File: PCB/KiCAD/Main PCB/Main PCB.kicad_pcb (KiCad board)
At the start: 2 copper layers, 118 x 118 mm, 127 parts, among them IC1 ADG608BRZ, IC2 ADG608BRZ, IC3 VNH7070ASTR, IC4 VNH7070ASTR, IC5 VNH7070ASTR, IC6 VNH7070ASTR, IC7 VNH7070ASTR, IC8 XB3-24Z8CM, J1 Conn_01x04, J2 Conn_01x04, J3 Conn_01x04, J4 Conn_01x04, J5 Conn_01x02, J6 Conn_01x02, J7 Conn_Coaxial_Small, J8 Conn_01x02, J9 Conn_01x02, M1 Conn_01x02, M2 Conn_01x02, M3 Conn_01x02, M4 Conn_01x02, Q1 BSS138, Q2 BSS138, U1 Teensy4.1, U2 Teensy4.0

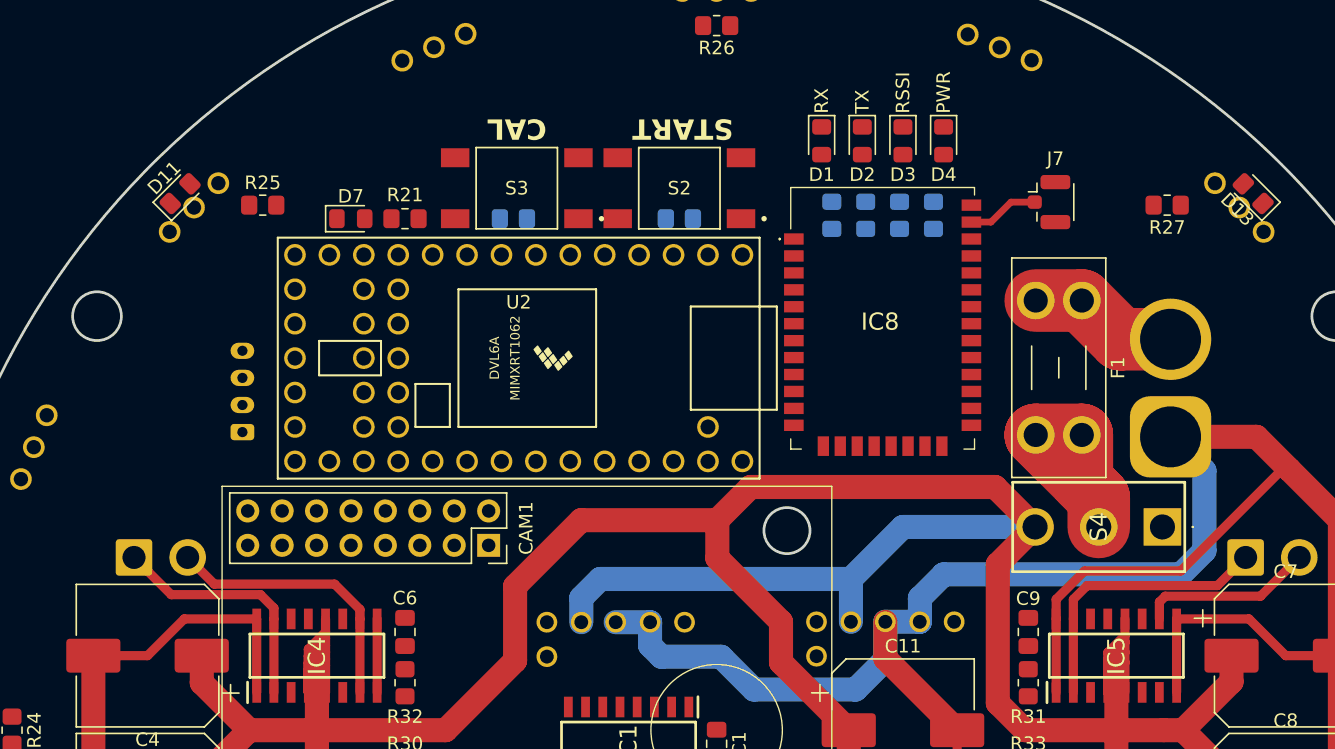
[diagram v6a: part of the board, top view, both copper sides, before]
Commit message: Changed to PCB and CAD
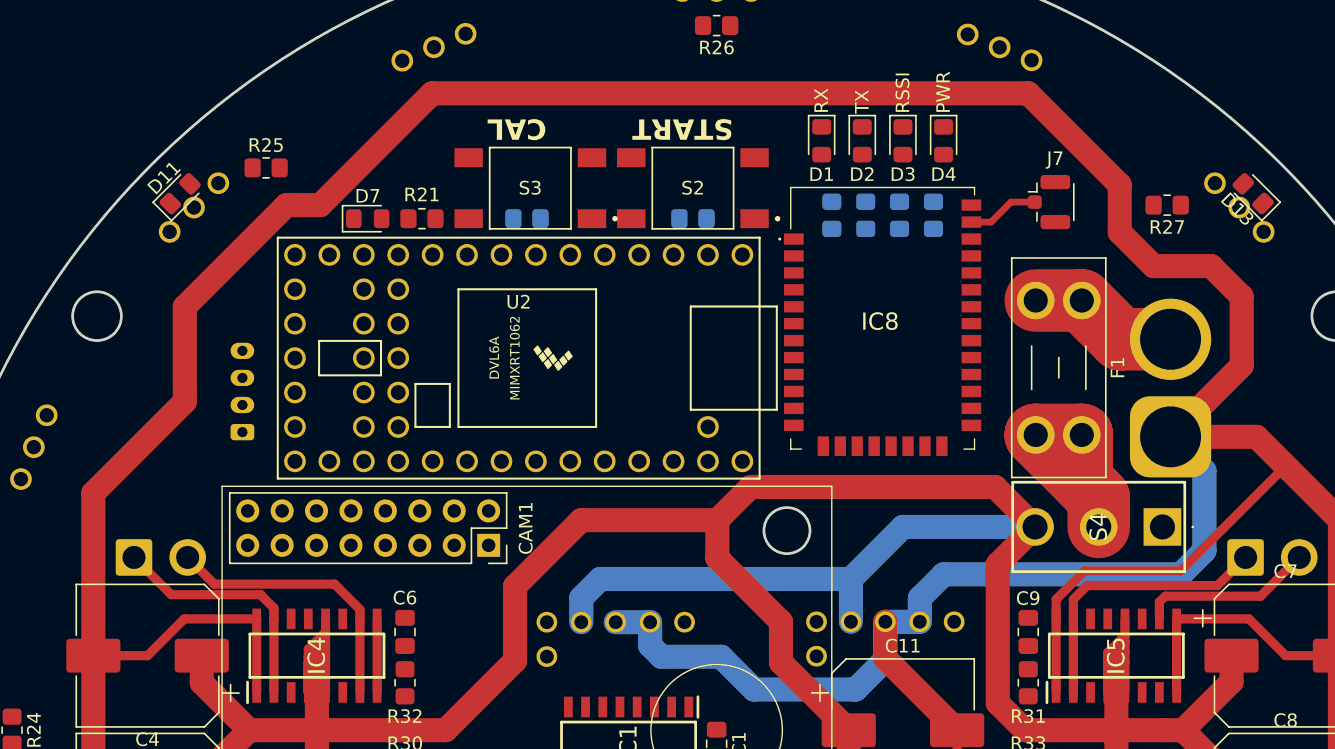
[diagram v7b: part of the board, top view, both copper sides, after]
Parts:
- moved R25 2.76 mm to (-33.2, -41.5)
- moved D7 1.25 mm to (-25.8, -37.8)
- moved R21 1.25 mm to (-21.8, -37.8)
- moved R3 1.00 mm to (-1.75, -37.8)
- moved R4 1.00 mm to (-14.0, -37.8)
- moved S2 1.00 mm to (-1.75, -40.0)
- moved S3 1.00 mm to (-13.8, -40.0)
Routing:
- net GND: track 351.7 -> 485.5 mm
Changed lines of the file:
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@@
 			(psa4output no)
 			(plot_black_and_white yes)
+			(plotinvisibletext no)
 			(sketchpadsonfab no)
 			(plotpadnumbers no)
@@
 	(footprint "TS04:SW_TS04-66-70-BK-260-SMT"
 		(layer "F.Cu")
-		(at -14.75 -40 180)
+		(at -13.75 -40 180)
 		(property "Reference" "S3"
 			(at 0 0 0)
@@
 	(footprint "Resistor_SMD:R_0805_2012Metric_Pad1.20x1.40mm_HandSolder"
 		(layer "F.Cu")
-		(at -33.5 -38.75)
+		(at -33.25 -41.5)
 		(descr "Resistor SMD 0805 (2012 Metric), square (rectangular) end terminal, IPC_7351 nominal with elongated pad for handsoldering. (Body size source: IPC-SM-782 page 72, https://www.pcb-3d.com/wordpress/wp-content/uploads/ipc-sm-782a_amendment_1_and_2.pdf), generated with kicad-footprint-generator")
 		(tags "resistor handsolder")
@@
 	(footprint "LED_SMD:LED_0805_2012Metric_Pad1.15x1.40mm_HandSolder"
 		(layer "F.Cu")
-		(at -27 -37.75)
+		(at -25.75 -37.75)
 		(descr "LED SMD 0805 (2012 Metric), square (rectangular) end terminal, IPC_7351 nominal, (Body size source: https://docs.google.com/spreadsheets/d/1BsfQQcO9C6DZCsRaXUlFlo91Tg2WpOkGARC1WS5S8t0/edit?usp=sharing), generated with kicad-footprint-generator")
 		(tags "LED handsolder")
@@
 	(footprint "TS04:SW_TS04-66-70-BK-260-SMT"
 		(layer "F.Cu")
-		(at -2.75 -40 180)
+		(at -1.75 -40 180)
 		(property "Reference" "S2"
 			(at 0 0 0)
@@
 	(footprint "Resistor_SMD:R_0805_2012Metric_Pad1.20x1.40mm_HandSolder"
 		(layer "F.Cu")
-		(at -23 -37.75 180)
+		(at -21.75 -37.75 180)
 		(descr "Resistor SMD 0805 (2012 Metric), square (rectangular) end terminal, IPC_7351 nominal with elongated pad for handsoldering. (Body size source: IPC-SM-782 page 72, https://www.pcb-3d.com/wordpress/wp-content/uploads/ipc-sm-782a_amendment_1_and_2.pdf), generated with kicad-footprint-generator")
 		(tags "resistor handsolder")
@@
 	(footprint "Resistor_SMD:R_0805_2012Metric_Pad1.20x1.40mm_HandSolder"
 		(layer "B.Cu")
-		(at -2.75 -37.75)
+		(at -1.75 -37.75)
 		(descr "Resistor SMD 0805 (2012 Metric), square (rectangular) end terminal, IPC_7351 nominal with elongated pad for handsoldering. (Body size source: IPC-SM-782 page 72, https://www.pcb-3d.com/wordpress/wp-content/uploads/ipc-sm-782a_amendment_1_and_2.pdf), generated with kicad-footprint-generator")
 		(tags "resistor handsolder")
@@
 	(footprint "Resistor_SMD:R_0805_2012Metric_Pad1.20x1.40mm_HandSolder"
 		(layer "B.Cu")
-		(at -15 -37.75)
+		(at -14 -37.75)
 		(descr "Resistor SMD 0805 (2012 Metric), square (rectangular) end terminal, IPC_7351 nominal with elongated pad for handsoldering. (Body size source: IPC-SM-782 page 72, https://www.pcb-3d.com/wordpress/wp-content/uploads/ipc-sm-782a_amendment_1_and_2.pdf), generated with kicad-footprint-generator")
 		(tags "resistor handsolder")
@@
 	)
 	(segment
+		(start -39.25 -24.25)
+		(end -39.25 -31.25)
+		(width 1.78)
+		(layer "F.Cu")
+		(net 1)
+	)
+	(segment
 		(start 25.055 -8.212)
 		(end 25.055 -2.788)
@@
 	)
 	(segment
+		(start -31.75 -38.75)
+		(end -29.25 -38.75)
+		(width 1.78)
+		(layer "F.Cu")
+		(net 1)
+	)
+	(segment
+		(start 32.25 -34.25)
+		(end 36.5 -34.25)
+		(width 1.78)
+		(layer "F.Cu")
+		(net 1)
+	)
+	(segment
 		(start -45 15)
 		(end -46 14)
@@
 	)
 	(segment
+		(start 38.75 -32)
+		(end 38.75 -26.9)
+		(width 1.78)
+		(layer "F.Cu")
+		(net 1)
+	)
+	(segment
 		(start 44.5 15.75)
 		(end 40 15.75)
@@
 	)
 	(segment
+		(start 38.75 -26.9)
+		(end 33.5 -21.65)
+		(width 1.78)
+		(layer "F.Cu")
+		(net 1)
+	)
+	(segment
+		(start 29.75 -40.25)
+		(end 29.75 -36.75)
+		(width 1.78)
+		(layer "F.Cu")
+		(net 1)
+	)
+	(segment
 		(start 41.75 -19.25)
 		(end 42.25 -19.25)
@@
 	)
 	(segment
+		(start -46 -17.5)
+		(end -39.25 -24.25)
+		(width 1.78)
+		(layer "F.Cu")
+		(net 1)
+	)
+	(segment
 		(start 27.1505 -11.75)
 		(end 34.25 -11.75)
@@
 	)
 	(segment
+		(start -21 -47)
+		(end 23 -47)
+		(width 1.78)
+		(layer "F.Cu")
+		(net 1)
+	)
+	(segment
 		(start 33.945 2.788)
 		(end 33.945 8.212)
@@
 	)
 	(segment
+		(start 36.5 -34.25)
+		(end 38.75 -32)
+		(width 1.78)
+		(layer "F.Cu")
+		(net 1)
+	)
+	(segment
 		(start 17.75 0.5)
 		(end 17.25 0)
@@
 	)
 	(segment
+		(start -46 -5.5)
+		(end -46 -17.5)
+		(width 1.78)
+		(layer "F.Cu")
+		(net 1)
+	)
+	(segment
 		(start -33.945 2.788)
 		(end -33.945 8.212)
@@
 	)
 	(segment
+		(start 29.75 -36.75)
+		(end 32.25 -34.25)
+		(width 1.78)
+		(layer "F.Cu")
+		(net 1)
+	)
+	(segment
 		(start 46 5.5)
 		(end 46 14.25)
@@
 	)
 	(segment
+		(start -29.25 -38.75)
+		(end -21 -47)
+		(width 1.78)
+		(layer "F.Cu")
+		(net 1)
+	)
+	(segment
 		(start 34.25 -11.75)
 		(end 41.75 -19.25)
@@
 	)
 	(segment
+		(start -39.25 -31.25)
+		(end -31.75 -38.75)
+		(width 1.78)
+		(layer "F.Cu")
+		(net 1)
+	)
+	(segment
 		(start -26.6505 11.25)
 		(end -35.5 11.25)
@@
 		(layer "F.Cu")
 		(net 1)
+	)
+	(segment
+		(start 23 -47)
+		(end 29.75 -40.25)
+		(width 1.78)
+		(layer "F.Cu")
+		(net 1)

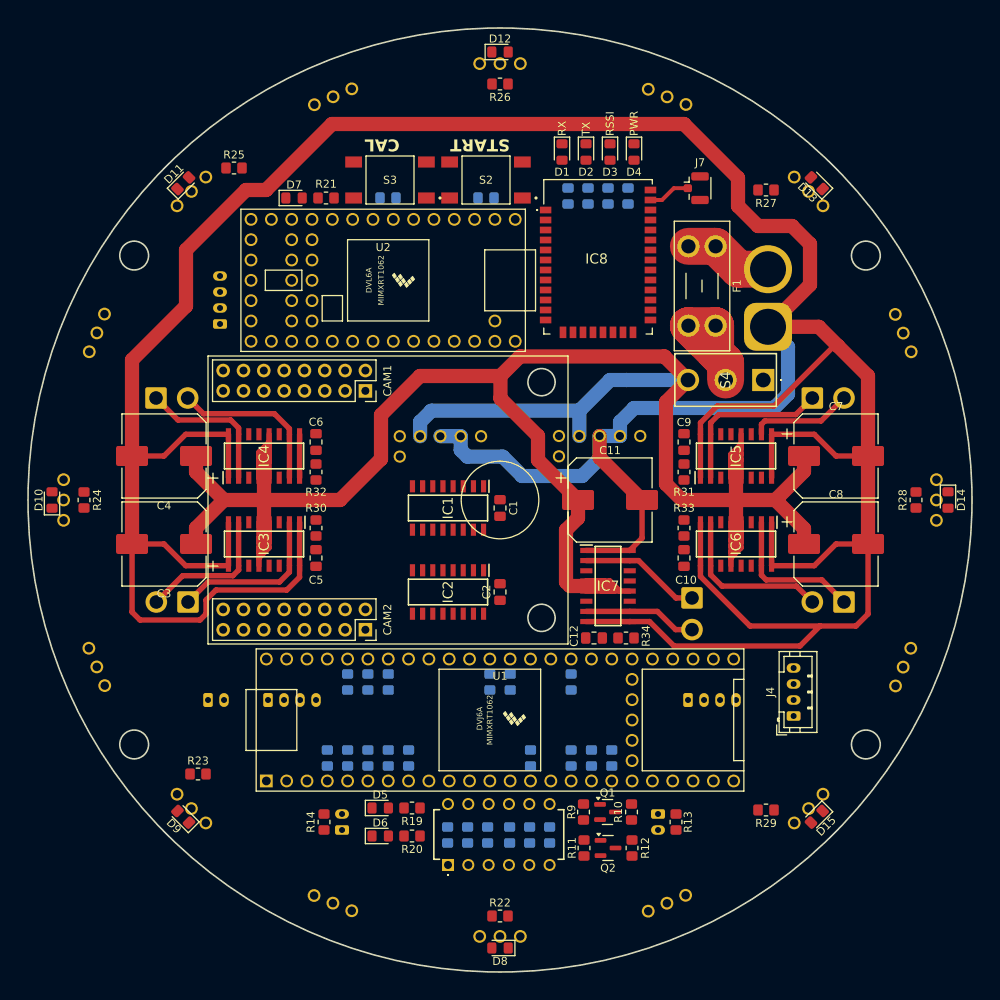
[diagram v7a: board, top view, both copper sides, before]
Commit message: Added kicker and spare serial and i2c
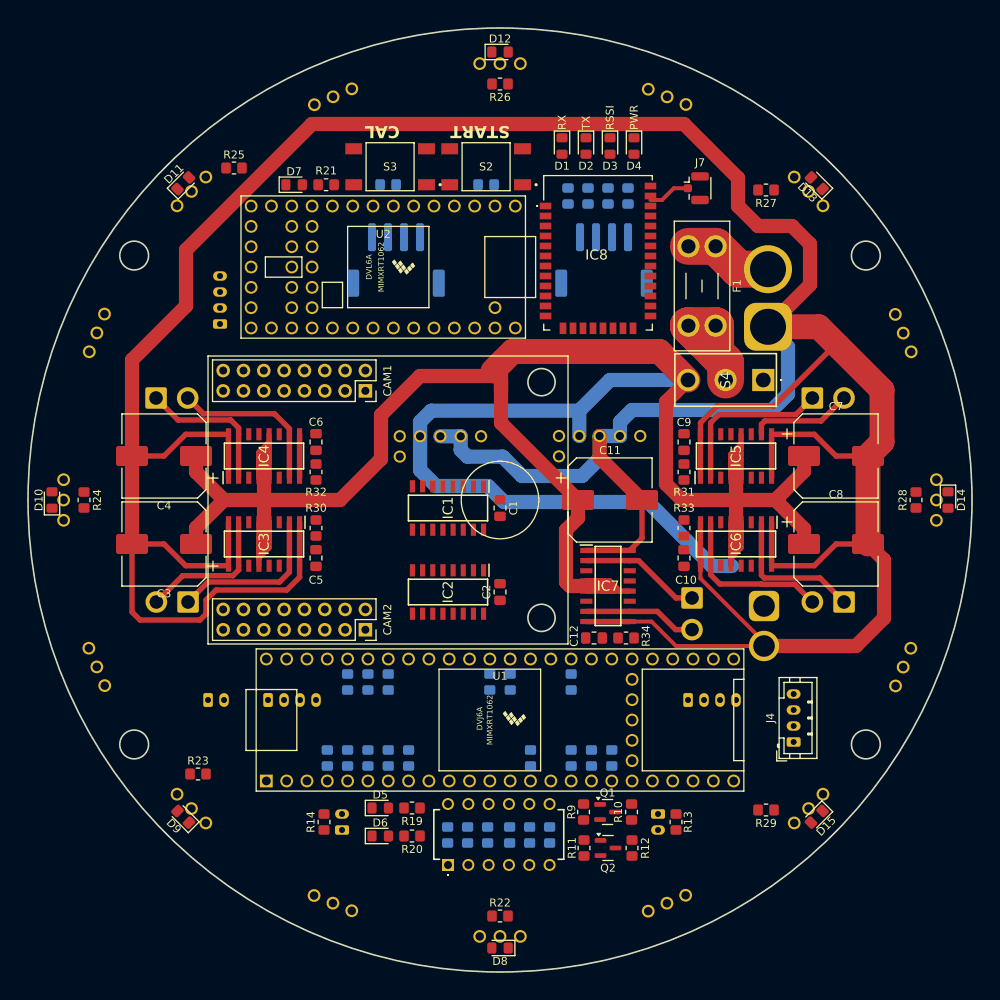
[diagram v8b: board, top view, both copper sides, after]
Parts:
- added J10: Conn_01x02, Connector_AMASS:AMASS_XT30U-M_1x02_P5.0mm_Vertical, B.Cu at (33.0, 13.2)
- added J11: Conn_01x04_MountingPin, Connector_JST:JST_PH_S4B-PH-SM4-TB_1x04-1MP_P2.00mm_Horizontal, B.Cu at (-13.0, -30.0)
- added J12: Conn_01x04_MountingPin, Connector_JST:JST_PH_S4B-PH-SM4-TB_1x04-1MP_P2.00mm_Horizontal, B.Cu at (13.0, -30.0)
- moved J4 3.25 mm to (36.7, 30.2)
- moved U2 1.66 mm to (-14.6, -29.1)
- moved D7 1.66 mm to (-25.7, -39.4)
- moved R21 1.66 mm to (-21.7, -39.4)
- moved R3 1.66 mm to (-1.74, -39.4)
- moved R4 1.66 mm to (-14.0, -39.4)
- moved S2 1.66 mm to (-1.74, -41.7)
- moved S3 1.66 mm to (-13.7, -41.7)
- moved D1 0.75 mm to (7.75, -44.2)
- moved D2 0.75 mm to (10.8, -44.2)
- moved D3 0.75 mm to (13.8, -44.2)
- moved D4 0.75 mm to (16.8, -44.2)
- moved IC8 0.50 mm to (12.2, -23.0)
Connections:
- U2 pad 35: unconnected-(U2-24_A10_TX6_SCL2-Pad35) -> SPARE_SCL
- U2 pad 36: unconnected-(U2-25_A11_RX6_SDA2-Pad36) -> SPARE_SDA
- U2 pad 39: unconnected-(U2-28_RX7-Pad39) -> SPARE_RX
- U2 pad 40: unconnected-(U2-29_TX7-Pad40) -> SPARE_TX
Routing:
- net +12V: track 327.9 -> 381.6 mm
- net GND: track 485.5 -> 484.6 mm
